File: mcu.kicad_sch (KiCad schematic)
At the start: 4 parts, among them Q4 NMOS, U4 ESP32-S3-WROOM-1

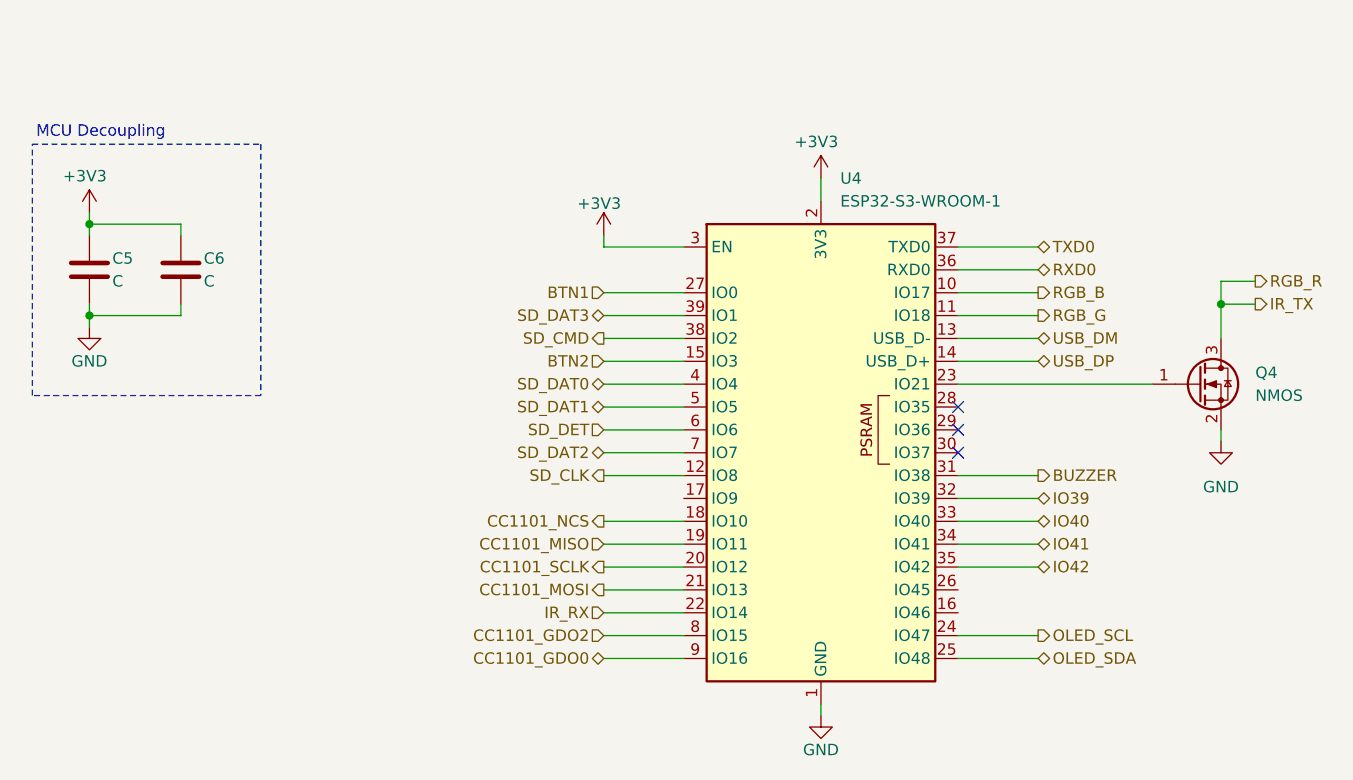
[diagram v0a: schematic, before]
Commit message: Add encoder to schematic
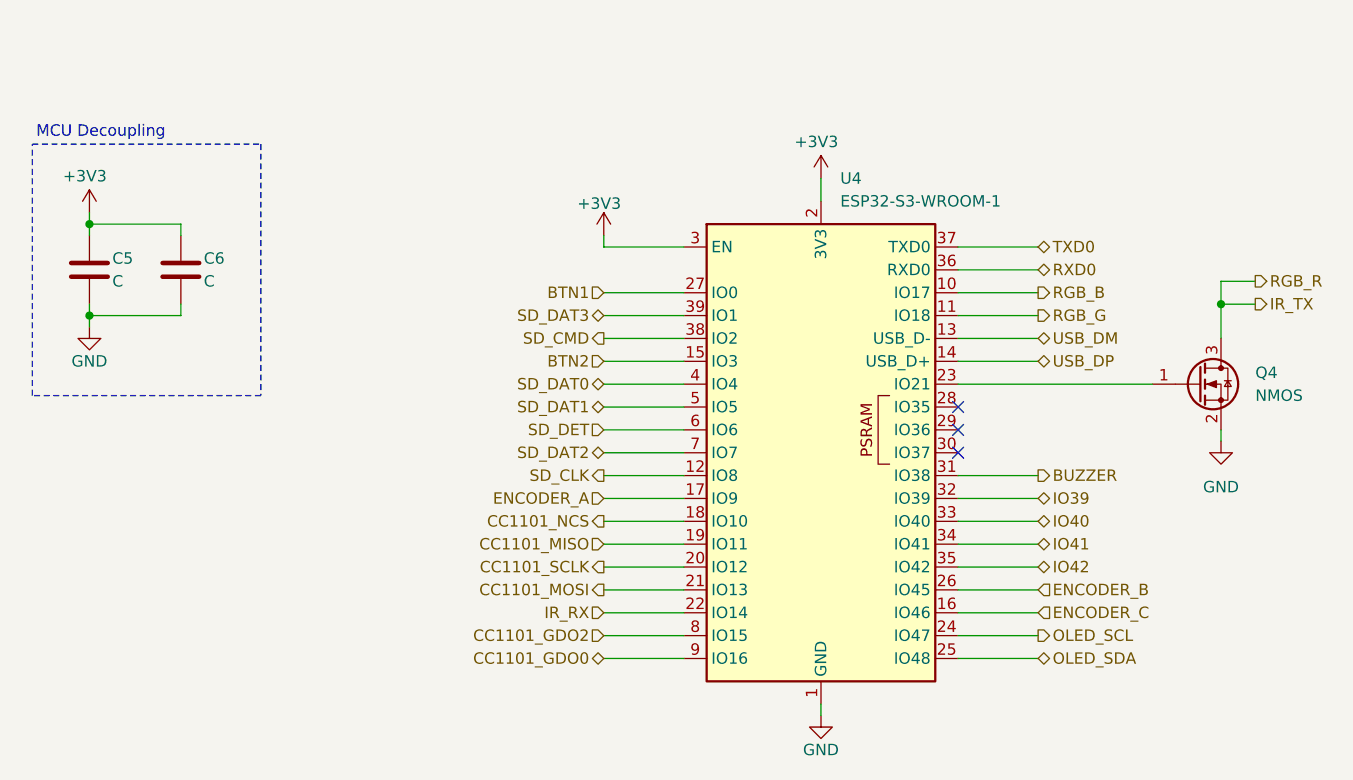
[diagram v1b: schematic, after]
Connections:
- net ENCODER_C: now reaches U4.16 (IO46)
- net ENCODER_A: now reaches U4.17 (IO9)
- net ENCODER_B: now reaches U4.26 (IO45)
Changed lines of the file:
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@@
+	(wire
+		(pts
+			(xy 83.82 60.96) (xy 92.71 60.96)
+		)
+		(stroke
+			(width 0)
+			(type default)
+		)
+	)
 	(wire
 		(pts
@@
 	(wire
 		(pts
+			(xy 123.19 71.12) (xy 132.08 71.12)
+		)
+		(stroke
+			(width 0)
+			(type default)
+		)
+	)
+	(wire
+		(pts
 			(xy 83.82 68.58) (xy 92.71 68.58)
 		)
@@
 		(pts
 			(xy 123.19 48.26) (xy 144.78 48.26)
+		)
+		(stroke
+			(width 0)
+			(type default)
+		)
+	)
+	(wire
+		(pts
+			(xy 123.19 73.66) (xy 132.08 73.66)
 		)
 		(stroke
@@
 		)
 	)
+	(hierarchical_label "ENCODER_B"
+		(shape input)
+		(at 132.08 71.12 0)
+		(effects
+			(font
+				(size 1.27 1.27)
+			)
+			(justify left)
+		)
+	)
+	(hierarchical_label "ENCODER_C"
+		(shape input)
+		(at 132.08 73.66 0)
+		(effects
+			(font
+				(size 1.27 1.27)
+			)
+			(justify left)
+		)
+	)
 	(hierarchical_label "RGB_R"
 		(shape output)
@@
 		)
 	)
+	(hierarchical_label "ENCODER_A"
+		(shape input)
+		(at 83.82 60.96 180)
+		(effects
+			(font
+				(size 1.27 1.27)
+			)
+			(justify right)
+		)
+	)

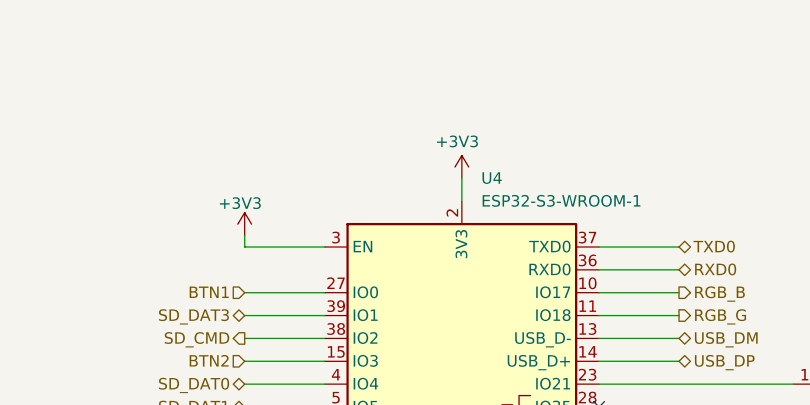
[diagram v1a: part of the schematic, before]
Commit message: Add bypass capacitors
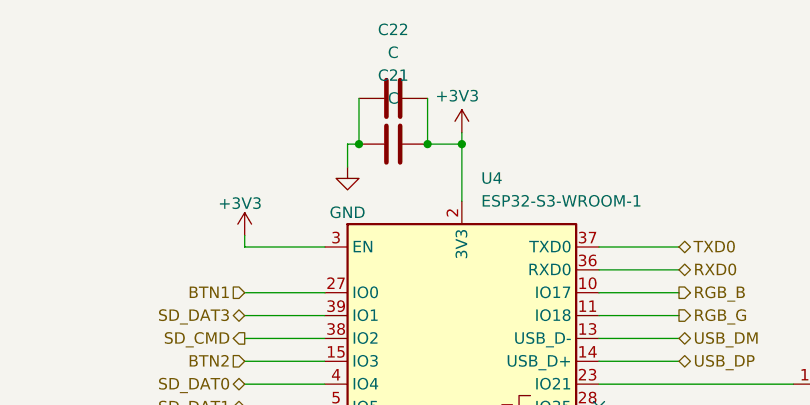
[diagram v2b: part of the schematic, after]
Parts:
- added C21, C22: C, Capacitor_SMD:C_0805_2012Metric, symbol Device:C
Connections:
- net +3V3: now also C21.2, C22.2
- net GND: now also C21.1, C22.1

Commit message: update pcb and schematic
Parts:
- removed C21, C22: C, Capacitor_SMD:C_0805_2012Metric, symbol Device:C

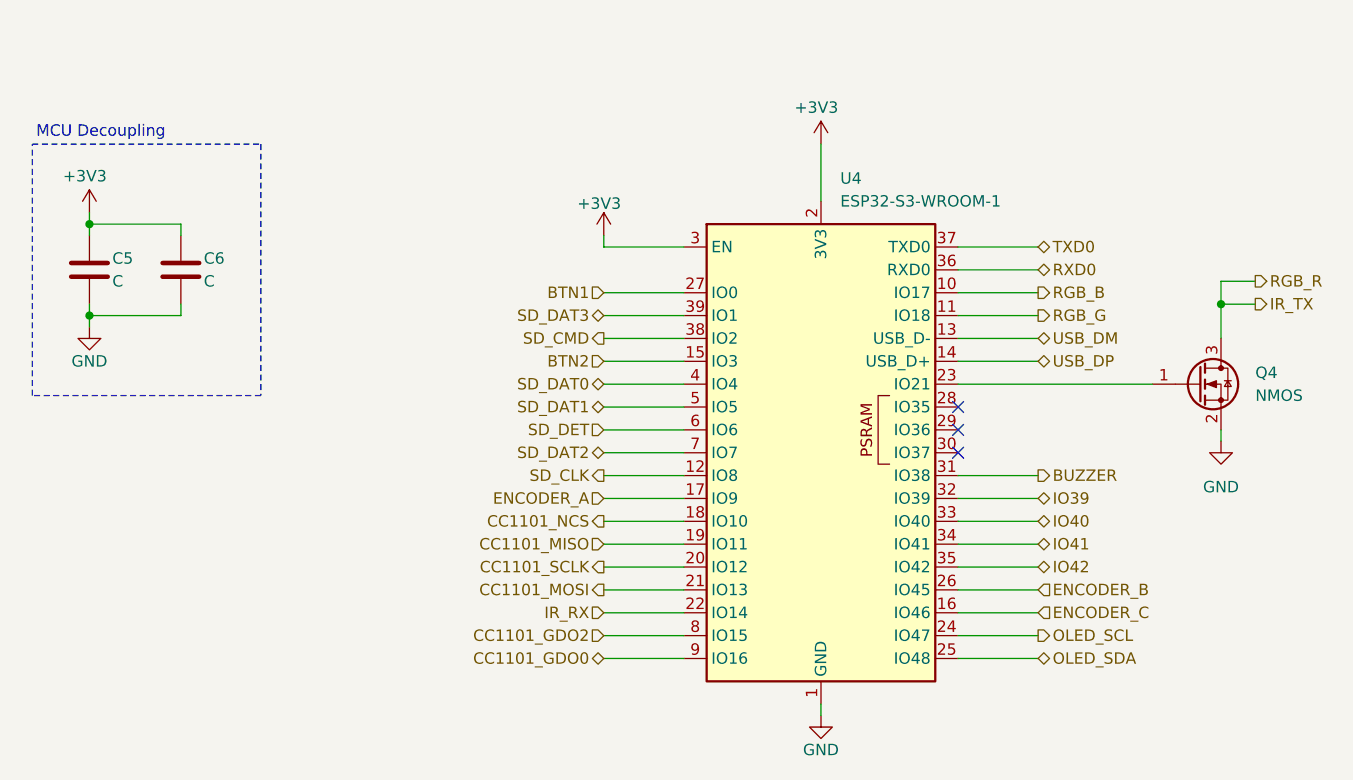
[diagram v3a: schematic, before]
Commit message: component routing
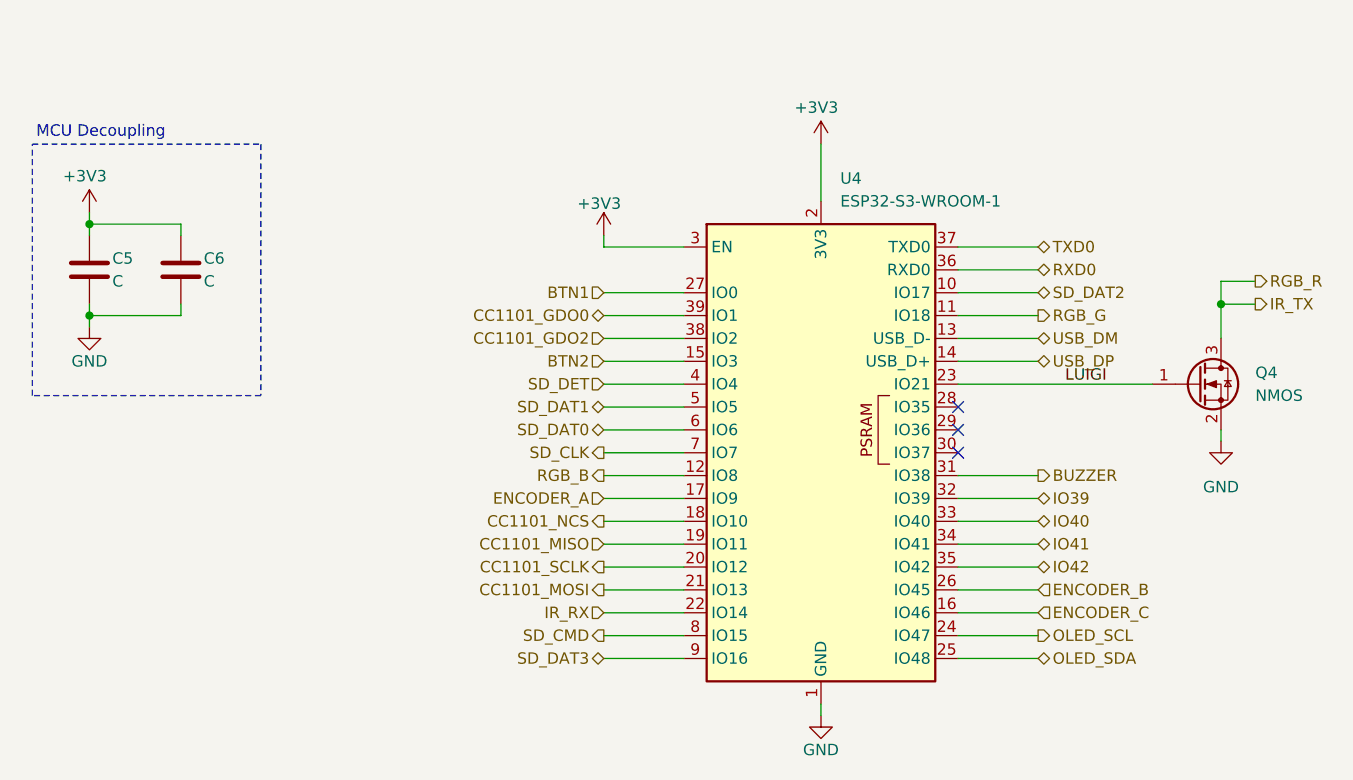
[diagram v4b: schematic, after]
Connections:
- net CC1101_GDO0: now also U4.39 (IO1); no longer U4.9 (IO16)
- net CC1101_GDO2: now also U4.38 (IO2); no longer U4.8 (IO15)
- net RGB_B: now also U4.12 (IO8); no longer U4.10 (IO17)
- net SD_CLK: now also U4.7 (IO7); no longer U4.12 (IO8)
- net SD_CMD: now also U4.8 (IO15); no longer U4.38 (IO2)
- net SD_DAT0: now also U4.6 (IO6); no longer U4.4 (IO4)
- net SD_DAT2: now also U4.10 (IO17); no longer U4.7 (IO7)
- net SD_DAT3: now also U4.9 (IO16); no longer U4.39 (IO1)
- net SD_DET: now also U4.4 (IO4); no longer U4.6 (IO6)
- net LUIGI: now reaches Q4.1 (G), U4.23 (IO21)

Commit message: finish routing
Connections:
- net USB_DM renamed USB_D-
- net USB_DP renamed USB_D+
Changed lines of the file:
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@@
 		)
 	)
-	(hierarchical_label "USB_DP"
+	(hierarchical_label "USB_D+"
 		(shape bidirectional)
 		(at 132.08 45.72 0)
@@
 		)
 	)
-	(hierarchical_label "USB_DM"
+	(hierarchical_label "USB_D-"
 		(shape bidirectional)
 		(at 132.08 43.18 0)

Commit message: LUIGI
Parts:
- C5: value C -> 100n
- C6: value C -> 10u
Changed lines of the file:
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@@
 			)
 		)
-		(property "Value" "C"
+		(property "Value" "100n"
 			(at 29.21 36.83 0)
 			(effects
@@
 			)
 		)
-		(property "Value" "C"
+		(property "Value" "10u"
 			(at 39.37 36.83 0)
 			(effects
